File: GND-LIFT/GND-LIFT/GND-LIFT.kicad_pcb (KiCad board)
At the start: 2 copper layers, 70 x 40 mm, 5 parts, among them J1 8191, J2 8191

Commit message: fix gnd-lift - add gerbers for gnd-lift & t-gnd
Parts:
- moved D1 2.00 mm to (86.0, 65.4)
- moved J1 1.50 mm to (118.5, 81.0)
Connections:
- C1 pad 1: /CHASSIS -> /PSU0V
- C1 pad 2: /PSU0V -> /CHASSIS
- J1 pad 1: /CHASSIS -> /PSU0V
- J2 pad 1: /PSU0V -> /CHASSIS
- R1 pad 1: /CHASSIS -> /PSU0V
- R1 pad 2: /PSU0V -> /CHASSIS
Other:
- board text added: "CHASSIS"
- board text added: "PSU0V"
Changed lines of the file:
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@@
       (plot_on_all_layers_selection 0x0000000_00000000)
       (disableapertmacros false)
-      (usegerberextensions false)
-      (usegerberattributes true)
-      (usegerberadvancedattributes true)
-      (creategerberjobfile true)
+      (usegerberextensions true)
+      (usegerberattributes false)
+      (usegerberadvancedattributes false)
+      (creategerberjobfile false)
       (dashed_line_dash_ratio 12.000000)
       (dashed_line_gap_ratio 3.000000)
@@
       (psa4output false)
       (plotreference true)
-      (plotvalue true)
+      (plotvalue false)
       (plotinvisibletext false)
       (sketchpadsonfab false)
-      (subtractmaskfromsilk false)
+      (subtractmaskfromsilk true)
       (outputformat 1)
       (mirror false)
-      (drillshape 1)
+      (drillshape 0)
       (scaleselection 1)
-      (outputdirectory "")
+      (outputdirectory "../Gerbers/")
     )
   )
@@
       (stroke (width 0.1) (type solid)) (layer "F.Fab"))
     (pad "1" thru_hole circle (at 0 0) (size 2 2) (drill 1) (layers "*.Cu" "*.Mask")
+      (net 2 "/PSU0V") (pintype "passive"))
+    (pad "2" thru_hole circle (at 10 0) (size 2 2) (drill 1) (layers "*.Cu" "*.Mask")
       (net 1 "/CHASSIS") (pintype "passive"))
-    (pad "2" thru_hole circle (at 10 0) (size 2 2) (drill 1) (layers "*.Cu" "*.Mask")
-      (net 2 "/PSU0V") (pintype "passive"))
     (model "${KICAD6_3DMODEL_DIR}/Capacitor_THT.3dshapes/C_Rect_L13.0mm_W6.0mm_P10.00mm_FKS3_FKP3_MKS4.wrl"
       (offset (xyz 0 0 0))
@@
       (stroke (width 0.2) (type default)) (layer "F.SilkS"))
     (pad "1" thru_hole circle (at -11 0 90) (size 2.4 2.4) (drill 1.2) (layers "*.Cu" "*.Mask")
+      (net 2 "/PSU0V") (pintype "passive"))
+    (pad "2" thru_hole oval (at 11 0 90) (size 2.4 2.4) (drill 1.2) (layers "*.Cu" "*.Mask")
       (net 1 "/CHASSIS") (pintype "passive"))
-    (pad "2" thru_hole oval (at 11 0 90) (size 2.4 2.4) (drill 1.2) (layers "*.Cu" "*.Mask")
-      (net 2 "/PSU0V") (pintype "passive"))
     (model "${KICAD6_3DMODEL_DIR}/Resistor_THT.3dshapes/R_Axial_DIN0918_L18.0mm_D9.0mm_P30.48mm_Horizontal.wrl"
       (offset (xyz 0 0 0))
@@
   )
   (footprint "Diode_THT:Diode_Bridge_28.6x28.6x7.3mm_P18.0mm_P11.6mm" (layer "F.Cu")
-    (at 84 65.4)
+    (at 86 65.4)
     (descr "Single phase bridge rectifier case 28.6x28.6mm, pitch 18.0mm & 11.6mm, see https://diotec.com/tl_files/diotec/files/pdf/datasheets/kbpc1500fw.pdf")
     (tags "Diode Bridge KBPCxxxxWP")
@@
       (stroke (width 0.127) (type solid)) (layer "F.Fab"))
     (pad "1" thru_hole circle (at -2.5 -3.505 90) (size 3.2 3.2) (drill 1.9) (layers "*.Cu" "*.Mask")
-      (net 2 "/PSU0V") (pinfunction "Pin_1") (pintype "passive") (solder_mask_margin 0.102))
+      (net 1 "/CHASSIS") (pinfunction "Pin_1") (pintype "passive") (solder_mask_margin 0.102))
     (pad "1" thru_hole circle (at -2.5 3.505 90) (size 3.2 3.2) (drill 1.9) (layers "*.Cu" "*.Mask")
-      (net 2 "/PSU0V") (pinfunction "Pin_1") (pintype "passive") (solder_mask_margin 0.102))
+      (net 1 "/CHASSIS") (pinfunction "Pin_1") (pintype "passive") (solder_mask_margin 0.102))
     (pad "1" thru_hole circle (at 0 -2.5 90) (size 3.2 3.2) (drill 1.5) (layers "*.Cu" "*.Mask")
-      (net 2 "/PSU0V") (pinfunction "Pin_1") (pintype "passive") (solder_mask_margin 0.102))
+      (net 1 "/CHASSIS") (pinfunction "Pin_1") (pintype "passive") (solder_mask_margin 0.102))
     (pad "1" thru_hole circle (at 0 2.5 90) (size 3.2 3.2) (drill 1.5) (layers "*.Cu" "*.Mask")
-      (net 2 "/PSU0V") (pinfunction "Pin_1") (pintype "passive") (solder_mask_margin 0.102))
+      (net 1 "/CHASSIS") (pinfunction "Pin_1") (pintype "passive") (solder_mask_margin 0.102))
     (pad "1" thru_hole circle (at 2.5 -3.505 90) (size 3.2 3.2) (drill 1.9) (layers "*.Cu" "*.Mask")
-      (net 2 "/PSU0V") (pinfunction "Pin_1") (pintype "passive") (solder_mask_margin 0.102))
+      (net 1 "/CHASSIS") (pinfunction "Pin_1") (pintype "passive") (solder_mask_margin 0.102))
     (pad "1" thru_hole circle (at 2.5 3.505 90) (size 3.2 3.2) (drill 1.9) (layers "*.Cu" "*.Mask")
-      (net 2 "/PSU0V") (pinfunction "Pin_1") (pintype "passive") (solder_mask_margin 0.102))
+      (net 1 "/CHASSIS") (pinfunction "Pin_1") (pintype "passive") (solder_mask_margin 0.102))
   )
   (footprint "CustomKicadFootprint:KEYSTONE_8191" (layer "F.Cu")
-    (at 117 81 90)
+    (at 118.5 81 90)
     (property "Sheetfile" "GND-LIFT.kicad_sch")
     (property "Sheetname" "")
@@
       (stroke (width 0.127) (type solid)) (layer "F.Fab"))
     (pad "1" thru_hole circle (at -2.5 -3.505 90) (size 3.2 3.2) (drill 1.9) (layers "*.Cu" "*.Mask")
-      (net 1 "/CHASSIS") (pinfunction "Pin_1") (pintype "passive") (solder_mask_margin 0.102))
+      (net 2 "/PSU0V") (pinfunction "Pin_1") (pintype "passive") (solder_mask_margin 0.102))
     (pad "1" thru_hole circle (at -2.5 3.505 90) (size 3.2 3.2) (drill 1.9) (layers "*.Cu" "*.Mask")
-      (net 1 "/CHASSIS") (pinfunction "Pin_1") (pintype "passive") (solder_mask_margin 0.102))
+      (net 2 "/PSU0V") (pinfunction "Pin_1") (pintype "passive") (solder_mask_margin 0.102))
     (pad "1" thru_hole circle (at 0 -2.5 90) (size 3.2 3.2) (drill 1.5) (layers "*.Cu" "*.Mask")
-      (net 1 "/CHASSIS") (pinfunction "Pin_1") (pintype "passive") (solder_mask_margin 0.102))
+      (net 2 "/PSU0V") (pinfunction "Pin_1") (pintype "passive") (solder_mask_margin 0.102))
     (pad "1" thru_hole circle (at 0 2.5 90) (size 3.2 3.2) (drill 1.5) (layers "*.Cu" "*.Mask")
-      (net 1 "/CHASSIS") (pinfunction "Pin_1") (pintype "passive") (solder_mask_margin 0.102))
+      (net 2 "/PSU0V") (pinfunction "Pin_1") (pintype "passive") (solder_mask_margin 0.102))
     (pad "1" thru_hole circle (at 2.5 -3.505 90) (size 3.2 3.2) (drill 1.9) (layers "*.Cu" "*.Mask")
-      (net 1 "/CHASSIS") (pinfunction "Pin_1") (pintype "passive") (solder_mask_margin 0.102))
+      (net 2 "/PSU0V") (pinfunction "Pin_1") (pintype "passive") (solder_mask_margin 0.102))
     (pad "1" thru_hole circle (at 2.5 3.505 90) (size 3.2 3.2) (drill 1.9) (layers "*.Cu" "*.Mask")
-      (net 1 "/CHASSIS") (pinfunction "Pin_1") (pintype "passive") (solder_mask_margin 0.102))
-  )
-  (gr_line (start 110 50) (end 110 86)
+      (net 2 "/PSU0V") (pinfunction "Pin_1") (pintype "passive") (solder_mask_margin 0.102))
+  )
+  (gr_line (start 111 50) (end 111 86)
     (stroke (width 0.25) (type default)) (layer "F.SilkS"))
-  (gr_line (start 81 50) (end 110 50)
+  (gr_line (start 81 50) (end 111 50)
     (stroke (width 0.25) (type default)) (layer "F.SilkS"))
-  (gr_line (start 110 86) (end 80 86)
+  (gr_line (start 111 86) (end 81 86)
     (stroke (width 0.25) (type default)) (layer "F.SilkS"))
   (gr_line (start 71 48) (end 141 48)
@@
     (effects (font (size 4 4) (thickness 0.5)) (justify bottom))
   )
+  (gr_text "CHASSIS" (at 125.5 56) (layer "F.SilkS")
+    (effects (font (size 1.5 1.5) (thickness 0.25) bold) (justify left bottom))
+  )
   (gr_text "~" (at 84 76) (layer "F.SilkS")
     (effects (font (size 4 4) (thickness 0.5)) (justify bottom))
   )
+  (gr_text "PSU0V" (at 123 86) (layer "F.SilkS")
+    (effects (font (size 2 2) (thickness 0.3)) (justify left bottom))
+  )
   (gr_text "10R 5W" (at 118 62 90) (layer "F.SilkS")
     (effects (font (size 1.75 2) (thickness 0.25)) (justify bottom))
@@
   )
   (via (at 136 52) (size 4.5) (drill 3.5) (layers "F.Cu" "B.Cu") (net 0))
-  (via (at 76 85) (size 4.5) (drill 3.5) (layers "F.Cu" "B.Cu") (net 0))
-  (via (at 93 68) (size 4.5) (drill 3.5) (layers "F.Cu" "B.Cu") (net 0))
+  (via (at 76 82) (size 4.5) (drill 3.5) (layers "F.Cu" "B.Cu") (net 0))
+  (via (at 95 68) (size 4.5) (drill 3.5) (layers "F.Cu" "B.Cu") (net 0))
   (via (at 136 82) (size 4.5) (drill 3.5) (layers "F.Cu" "B.Cu") (net 0))
-  (via (at 76 51) (size 4.5) (drill 3.5) (layers "F.Cu" "B.Cu") (net 0))
+  (via (at 76 52) (size 4.5) (drill 3.5) (layers "F.Cu" "B.Cu") (net 0))
   (zone (net 2) (net_name "/PSU0V") (layers "F&B.Cu") (hatch edge 0.5)
     (connect_pads yes (clearance 0.5))
@@
     (polygon
       (pts
-        (xy 82 63)
-        (xy 82 67)
-        (xy 90 73)
-        (xy 90 87)
+        (xy 84 63)
+        (xy 84 67)
+        (xy 92 73)
+        (xy 92 87)
         (xy 124 87)
         (xy 124 77)
@@
     (polygon
       (pts
-        (xy 87 86)
-        (xy 87 76)
+        (xy 89 86)
+        (xy 89 76)
         (xy 79 68)
         (xy 79 61)
@@
         (xy 118 49)
         (xy 80 49)
-        (xy 79 54)
-        (xy 74 64)
-        (xy 74 75)
-        (xy 78 81)
-        (xy 82 86)
+        (xy 80 55)
+        (xy 75 57)
+        (xy 75 75)
+        (xy 80 81)
+        (xy 84 86)
       )
     )

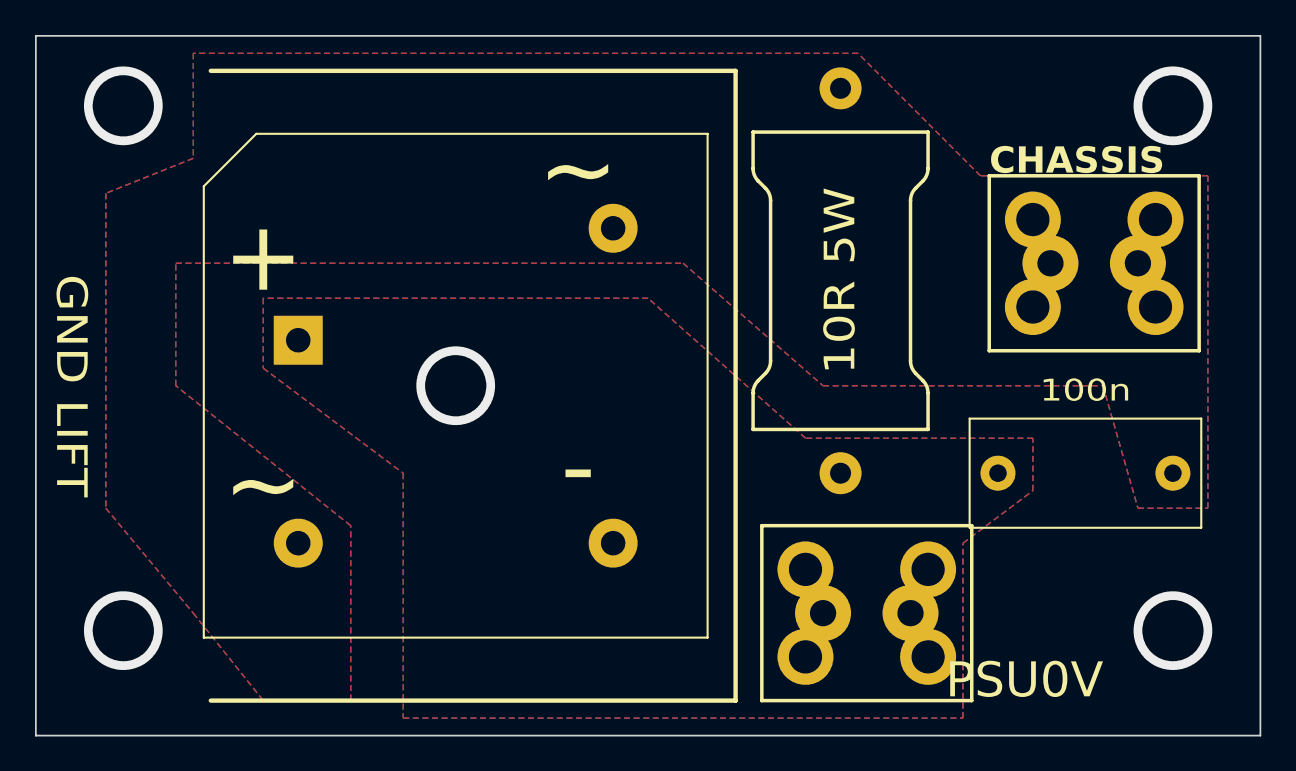
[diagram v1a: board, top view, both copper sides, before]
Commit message: gnd-lift rev1.1
fix silkscreen
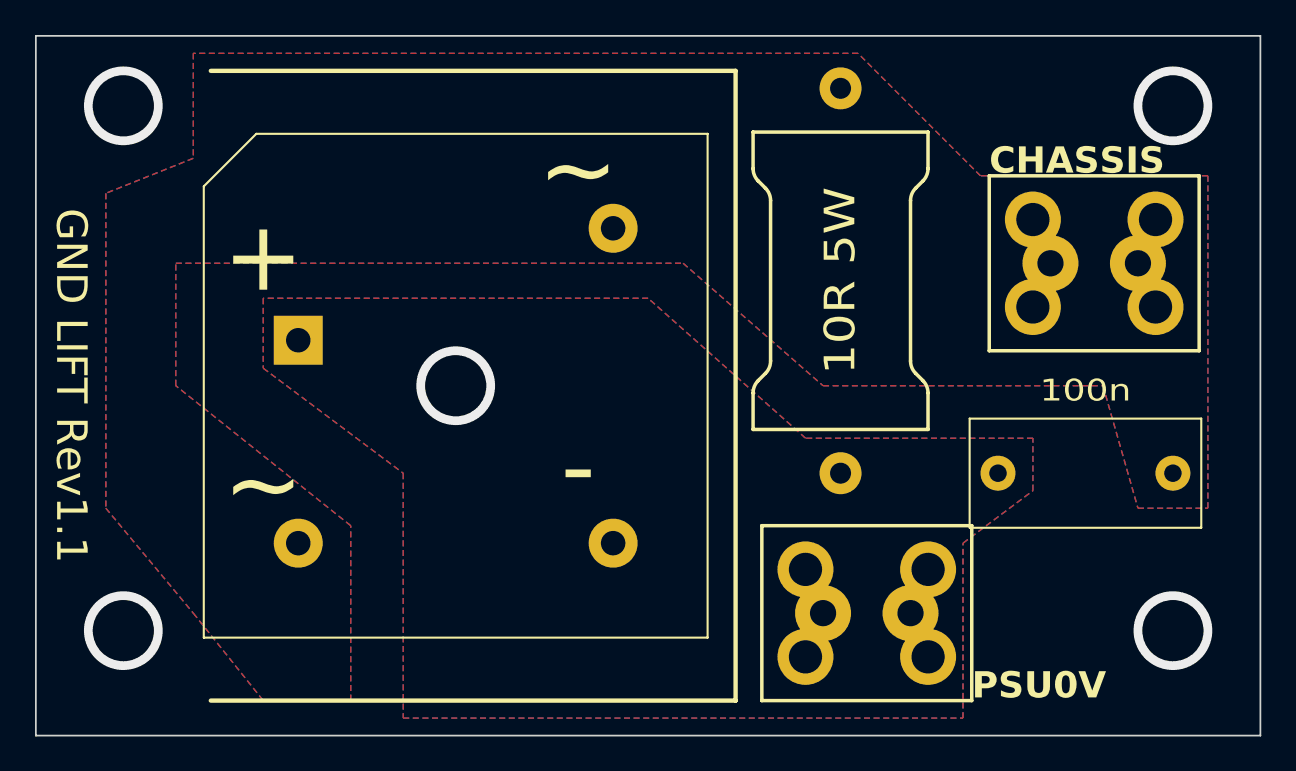
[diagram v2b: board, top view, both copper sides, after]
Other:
- board text added: "GND LIFT Rev1.1"
- board text removed: "GND LIFT"
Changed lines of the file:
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@@
     (effects (font (size 4 4) (thickness 0.5)) (justify bottom))
   )
-  (gr_text "PSU0V" (at 123 86) (layer "F.SilkS")
-    (effects (font (size 2 2) (thickness 0.3)) (justify left bottom))
+  (gr_text "PSU0V" (at 124.5 86) (layer "F.SilkS")
+    (effects (font (size 1.5 1.5) (thickness 0.25) bold) (justify left bottom))
   )
   (gr_text "10R 5W" (at 118 62 90) (layer "F.SilkS")
@@
     (effects (font (size 4 4) (thickness 0.5)) (justify bottom))
   )
-  (gr_text "GND LIFT" (at 72 68 -90) (layer "F.SilkS")
-    (effects (font (size 1.75 2) (thickness 0.25)) (justify bottom))
+  (gr_text "GND LIFT Rev1.1" (at 72 68 270) (layer "F.SilkS")
+    (effects (font (size 1.75 1.75) (thickness 0.25)) (justify bottom))
   )
   (gr_text "~" (at 102 58) (layer "F.SilkS")
